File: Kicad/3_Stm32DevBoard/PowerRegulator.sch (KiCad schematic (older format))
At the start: 13 parts, among them J5 PowerTest_PinHeader, J6 9V Power JST XH, U1 AMS1117-5.0, U2 AMS1117-3.3

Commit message: STM32 Dev Board
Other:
- moved on the sheet: J5
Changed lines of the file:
@@
-$EndComp
-$Comp
-L Regulator_Linear:AMS1117-3.3 U?
-U 1 1 5E8DF986
-P 4550 3850
-AR Path="/5E8DF986" Ref="U?"  Part="1"
-AR Path="/5E8D81C7/5E8DF986" Ref="U2"  Part="1"
-F 0 "U2" H 4550 4092 50  0000 C CNN
-F 1 "AMS1117-3.3" H 4550 4001 50  0000 C CNN
-F 2 "Package_TO_SOT_SMD:SOT-223-3_TabPin2" H 4550 4050 50  0001 C CNN
-F 3 "http://www.advanced-monolithic.com/pdf/ds1117.pdf" H 4650 3600 50  0001 C CNN
-	1    4550 3850
-	1    0    0    -1
 $EndComp
 $Comp
@@
 $Comp
 L power:GND #PWR?
-U 1 1 5E8DF9B0
-P 5100 4150
-AR Path="/5E8DF9B0" Ref="#PWR?"  Part="1"
-AR Path="/5E8D81C7/5E8DF9B0" Ref="#PWR016"  Part="1"
-F 0 "#PWR016" H 5100 3900 50  0001 C CNN
-F 1 "GND" H 5105 3977 50  0000 C CNN
-F 2 "" H 5100 4150 50  0001 C CNN
-F 3 "" H 5100 4150 50  0001 C CNN
-	1    5100 4150
-	1    0    0    -1
-$EndComp
-$Comp
-L power:GND #PWR?
 U 1 1 5E8DF9B6
 P 5100 3100
@@
 $EndComp
 Wire Wire Line
-	4850 3850 5100 3850
-Wire Wire Line
 	4850 2800 5100 2800
-Wire Wire Line
-	4250 3850 4100 3850
 Wire Wire Line
 	3550 2800 3550 2850
@@
 	1    0    0    -1
 $EndComp
-$Comp
-L power:GND #PWR?
-U 1 1 5E8DF9C9
-P 4550 4150
-AR Path="/5E8DF9C9" Ref="#PWR?"  Part="1"
-AR Path="/5E8D81C7/5E8DF9C9" Ref="#PWR012"  Part="1"
-F 0 "#PWR012" H 4550 3900 50  0001 C CNN
-F 1 "GND" H 4555 3977 50  0000 C CNN
-F 2 "" H 4550 4150 50  0001 C CNN
-F 3 "" H 4550 4150 50  0001 C CNN
-	1    4550 4150
-	1    0    0    -1
-$EndComp
 Text Notes 3000 3450 0    31   ~ 0
 Vfw = 2 V\n I = (9-2)/1 = 7 mA
 Text Notes 5500 2900 0    31   ~ 0
 5V: LCD: about 60 mA\nPd = (9 V - 5V) * 60 mA = 240 mW\nTj = Ta(max) + Pd * (Thermal Resistance (junction-to-ambient) =\n125 = 30 + Pd * 70 => 1.36 W\nNo heat sink needed
-Text Notes 5500 3900 0    31   ~ 0
-3.3V: STM32: about 100 mA \nPd = (9 V - 3.3V) * 100 mA = 570 mW\nTj = Ta(max) + Pd * (Thermal Resistance (junction-to-ambient) =\n125 = 30 + Pd * 70 => 1.36 W\nNo heat sink needed
-Connection ~ 4100 3850
 $Comp
 L power:+5V #PWR?
@@
 Wire Wire Line
 	4100 2800 4250 2800
-$Comp
-L power:+3V3 #PWR?
-U 1 1 5E8DF9EC
-P 5100 3850
-AR Path="/5E8DF9EC" Ref="#PWR?"  Part="1"
-AR Path="/5E8D81C7/5E8DF9EC" Ref="#PWR015"  Part="1"
-F 0 "#PWR015" H 5100 3700 50  0001 C CNN
-F 1 "+3V3" H 5115 4023 50  0000 C CNN
-F 2 "" H 5100 3850 50  0001 C CNN
-F 3 "" H 5100 3850 50  0001 C CNN
-	1    5100 3850
-	1    0    0    -1
-$EndComp
 Text Notes 3500 1000 0    50   ~ 10
 Power Regulator\n\n
@@
 L power:+5V #PWR0103
 U 1 1 5FACFDD8
-P 1900 3450
-F 0 "#PWR0103" H 1900 3300 50  0001 C CNN
-F 1 "+5V" H 1915 3623 50  0000 C CNN
-F 2 "" H 1900 3450 50  0001 C CNN
-F 3 "" H 1900 3450 50  0001 C CNN
-	1    1900 3450
+P 2050 3700
+F 0 "#PWR0103" H 2050 3550 50  0001 C CNN
+F 1 "+5V" H 2065 3873 50  0000 C CNN
+F 2 "" H 2050 3700 50  0001 C CNN
+F 3 "" H 2050 3700 50  0001 C CNN
+	1    2050 3700
 	1    0    0    -1
 $EndComp
@@
 L power:+3V3 #PWR0104
 U 1 1 5FAD14EB
-P 2100 3550
-F 0 "#PWR0104" H 2100 3400 50  0001 C CNN
-F 1 "+3V3" H 2115 3723 50  0000 C CNN
-F 2 "" H 2100 3550 50  0001 C CNN
-F 3 "" H 2100 3550 50  0001 C CNN
-	1    2100 3550
+P 2250 3800
+F 0 "#PWR0104" H 2250 3650 50  0001 C CNN
+F 1 "+3V3" H 2265 3973 50  0000 C CNN
+F 2 "" H 2250 3800 50  0001 C CNN
+F 3 "" H 2250 3800 50  0001 C CNN
+	1    2250 3800
 	1    0    0    -1
 $EndComp
@@
 L power:GND #PWR?
 U 1 1 5FAD2482
-P 1200 3650
+P 1350 3900
 AR Path="/5FAD2482" Ref="#PWR?"  Part="1"
 AR Path="/5E8D81C7/5FAD2482" Ref="#PWR0105"  Part="1"
-F 0 "#PWR0105" H 1200 3400 50  0001 C CNN
-F 1 "GND" H 1205 3477 50  0000 C CNN
-F 2 "" H 1200 3650 50  0001 C CNN
-F 3 "" H 1200 3650 50  0001 C CNN
-	1    1200 3650
+F 0 "#PWR0105" H 1350 3650 50  0001 C CNN
+F 1 "GND" H 1355 3727 50  0000 C CNN
+F 2 "" H 1350 3900 50  0001 C CNN
+F 3 "" H 1350 3900 50  0001 C CNN
+	1    1350 3900
 	1    0    0    -1
 $EndComp
@@
 $EndComp
 $Comp
-L Device:CP1 C4
-U 1 1 5E99E117
-P 5100 4000
-F 0 "C4" H 5215 4046 50  0000 L CNN
-F 1 "22uF" H 5215 3955 50  0000 L CNN
-F 2 "Diode_SMD:D_SMB_Handsoldering" H 5100 4000 50  0001 C CNN
-F 3 "~" H 5100 4000 50  0001 C CNN
-	1    5100 4000
-	1    0    0    -1
-$EndComp
-Connection ~ 5100 3850
-$Comp
 L Device:CP1 C3
 U 1 1 5E99F224
@@
 L Connector:Conn_01x04_Male J5
 U 1 1 5E90BAA0
-P 1000 3450
-F 0 "J5" H 1108 3731 50  0000 C CNN
-F 1 "PowerTest_PinHeader" H 1108 3640 50  0000 C CNN
-F 2 "Connector_PinHeader_2.54mm:PinHeader_1x04_P2.54mm_Vertical" H 1000 3450 50  0001 C CNN
-F 3 "~" H 1000 3450 50  0001 C CNN
-	1    1000 3450
-	1    0    0    -1
-$EndComp
-Wire Wire Line
-	1200 3550 2100 3550
-Wire Wire Line
-	1900 3450 1200 3450
-Wire Wire Line
-	1200 3350 1700 3350
-$Comp
-L power:+9V #PWR0112
-U 1 1 5EAD02BC
-P 1700 3350
-F 0 "#PWR0112" H 1700 3200 50  0001 C CNN
-F 1 "+9V" H 1715 3523 50  0000 C CNN
-F 2 "" H 1700 3350 50  0001 C CNN
-F 3 "" H 1700 3350 50  0001 C CNN
-	1    1700 3350
-	1    0    0    -1
-$EndComp
+P 1150 3700
+F 0 "J5" H 1258 3981 50  0000 C CNN
+F 1 "PowerTest_PinHeader" H 1258 3890 50  0000 C CNN
+F 2 "Connector_PinHeader_2.54mm:PinHeader_1x04_P2.54mm_Vertical" H 1150 3700 50  0001 C CNN
+F 3 "~" H 1150 3700 50  0001 C CNN
+	1    1150 3700
+	1    0    0    -1
+$EndComp
+Wire Wire Line
+	1350 3800 2250 3800
+Wire Wire Line
+	2050 3700 1350 3700
+Wire Wire Line
+	1350 3600 1850 3600
 Wire Wire Line
 	1250 1250 1550 1250
@@
 Wire Wire Line
 	1550 1250 1700 1250
-Wire Wire Line
-	4100 3850 4100 4550
 Wire Notes Line
 	7400 5200 7400 550
@@
 Text Notes 5500 3100 0    31   ~ 0
 22 uF Tantalum advised ->\n47 uf Tantalum in inventory instead
-Text Notes 5500 4100 0    31   ~ 0
-22 uF Tantalum advised ->\n47 uf Tantalum in inventory instead
 $Comp
 L power:+9V #PWR0114
@@
 	3550 2550 3550 2800
 Wire Wire Line
-	4100 2950 4100 3850
-Wire Wire Line
-	4100 2800 4100 3850
-Wire Wire Line
 	3450 2800 3550 2800
 Text HLabel 3450 2800 0    50   Input ~ 0
@@
 Text Notes 4250 2500 0    50   ~ 0
 Model: BLM21AG102SN1D'\nSpecs: 600 mA, 25% 1 KOhm, 100 MHz, 0805\nAccording AliExpress: 200 mA
+Wire Wire Line
+	4100 2800 4100 3850
+$Comp
+L Device:CP1 C4
+U 1 1 5E99E117
+P 5100 4000
+F 0 "C4" H 5215 4046 50  0000 L CNN
+F 1 "22uF" H 5215 3955 50  0000 L CNN
+F 2 "Diode_SMD:D_SMB_Handsoldering" H 5100 4000 50  0001 C CNN
+F 3 "~" H 5100 4000 50  0001 C CNN
+	1    5100 4000
+	1    0    0    -1
+$EndComp
+$Comp
+L power:+3V3 #PWR?
+U 1 1 5E8DF9EC
+P 5100 3850
+AR Path="/5E8DF9EC" Ref="#PWR?"  Part="1"
+AR Path="/5E8D81C7/5E8DF9EC" Ref="#PWR015"  Part="1"
+F 0 "#PWR015" H 5100 3700 50  0001 C CNN
+F 1 "+3V3" H 5115 4023 50  0000 C CNN
+F 2 "" H 5100 3850 50  0001 C CNN
+F 3 "" H 5100 3850 50  0001 C CNN
+	1    5100 3850
+	1    0    0    -1
+$EndComp
+$Comp
+L power:GND #PWR?
+U 1 1 5E8DF9C9
+P 4550 4150
+AR Path="/5E8DF9C9" Ref="#PWR?"  Part="1"
+AR Path="/5E8D81C7/5E8DF9C9" Ref="#PWR012"  Part="1"
+F 0 "#PWR012" H 4550 3900 50  0001 C CNN
+F 1 "GND" H 4555 3977 50  0000 C CNN
+F 2 "" H 4550 4150 50  0001 C CNN
+F 3 "" H 4550 4150 50  0001 C CNN
+	1    4550 4150
+	1    0    0    -1
+$EndComp
+Wire Wire Line
+	4100 2950 4100 3850
+Wire Wire Line
+	4100 3850 4100 4550
+Connection ~ 4100 3850
+Wire Wire Line
+	4250 3850 4100 3850
+Connection ~ 5100 3850
+Wire Wire Line
+	4850 3850 5100 3850
+$Comp
+L power:GND #PWR?
+U 1 1 5E8DF9B0
+P 5100 4150
+AR Path="/5E8DF9B0" Ref="#PWR?"  Part="1"
+AR Path="/5E8D81C7/5E8DF9B0" Ref="#PWR016"  Part="1"
+F 0 "#PWR016" H 5100 3900 50  0001 C CNN
+F 1 "GND" H 5105 3977 50  0000 C CNN
+F 2 "" H 5100 4150 50  0001 C CNN
+F 3 "" H 5100 4150 50  0001 C CNN
+	1    5100 4150
+	1    0    0    -1
+$EndComp
+$Comp
+L Regulator_Linear:AMS1117-3.3 U?
+U 1 1 5E8DF986
+P 4550 3850
+AR Path="/5E8DF986" Ref="U?"  Part="1"
+AR Path="/5E8D81C7/5E8DF986" Ref="U2"  Part="1"
+F 0 "U2" H 4550 4092 50  0000 C CNN
+F 1 "AMS1117-3.3" H 4550 4001 50  0000 C CNN
+F 2 "Package_TO_SOT_SMD:SOT-223-3_TabPin2" H 4550 4050 50  0001 C CNN
+F 3 "http://www.advanced-monolithic.com/pdf/ds1117.pdf" H 4650 3600 50  0001 C CNN
+	1    4550 3850
+	1    0    0    -1
+$EndComp
+Text Notes 5500 4100 0    31   ~ 0
+22 uF Tantalum advised ->\n47 uf Tantalum in inventory instead
+Text Notes 5500 3900 0    31   ~ 0
+3.3V: STM32: about 100 mA \nPd = (9 V - 3.3V) * 100 mA = 570 mW\nTj = Ta(max) + Pd * (Thermal Resistance (junction-to-ambient) =\n125 = 30 + Pd * 70 => 1.36 W\nNo heat sink needed
+Text HLabel 1850 3600 1    50   Input ~ 0
++9V_SAFE
 $EndSCHEMATC

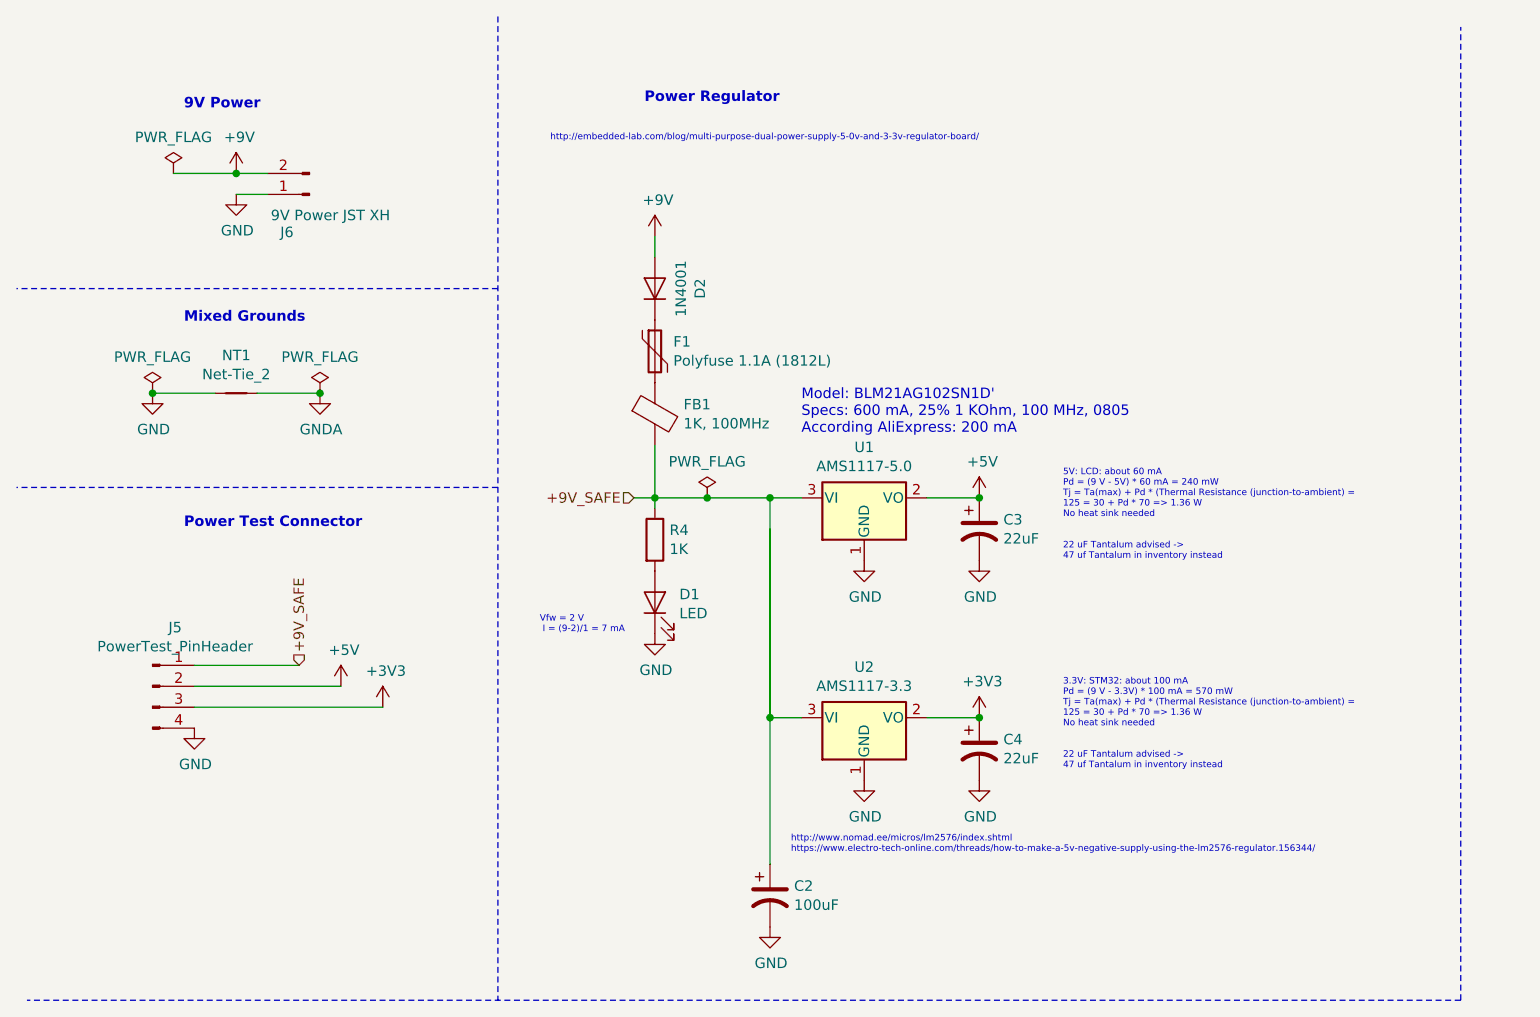
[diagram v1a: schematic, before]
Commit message: Remove 3V3 voltage regulation (get from STM32 5V)
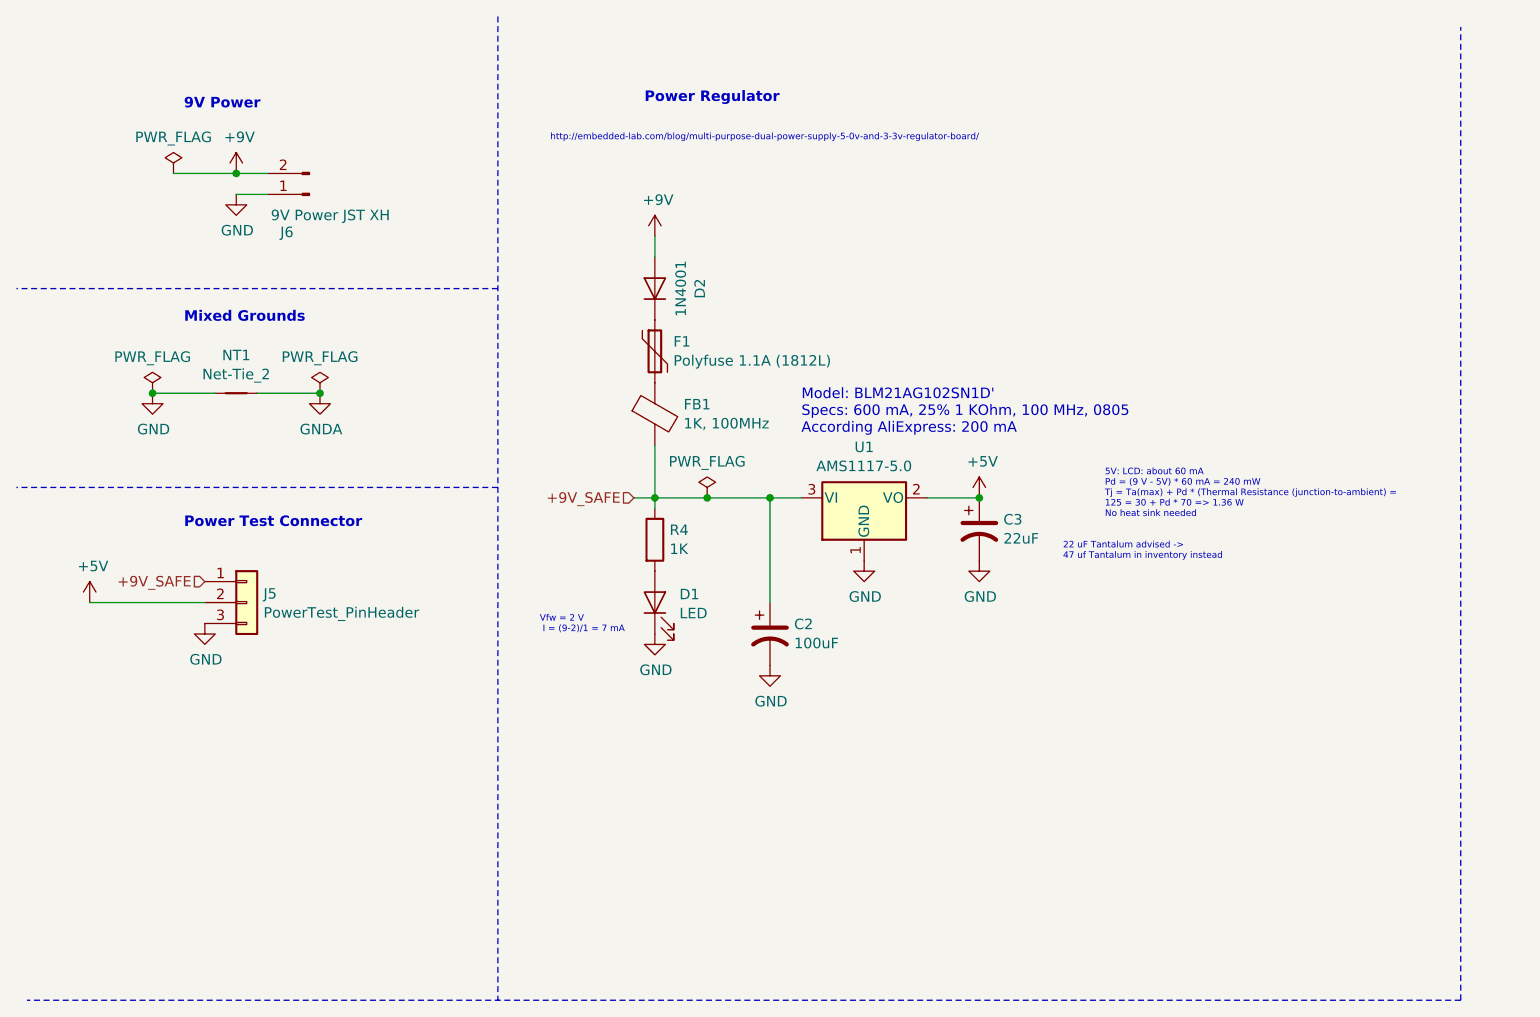
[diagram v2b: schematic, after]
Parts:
- removed C4: 22uF, Diode_SMD:D_SMB_Handsoldering, symbol Device:CP1
- removed J5: PowerTest_PinHeader, Connector_PinHeader_2.54mm:PinHeader_1x04_P2.54mm_Vertical, symbol Connector:Conn_01x04_Male
- removed U2: AMS1117-3.3, Package_TO_SOT_SMD:SOT-223-3_TabPin2, symbol Regulator_Linear:AMS1117-3.3
- added J5: PowerTest_PinHeader, Connector_PinHeader_2.54mm:PinHeader_1x03_P2.54mm_Vertical, symbol Connector_Generic:Conn_01x03
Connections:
- net labels removed: +3V3
- wire segments 21 -> 15
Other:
- note removed: "3.3V: STM32: about 100 mA \nPd = (9 V - 3.3V) * 100 mA = 570 mW\nTj = Ta(max) + Pd * (Thermal Resistance (junction-to-ambient) =\n125 = 30 + Pd * 70 => 1.36 W\nNo heat sink needed"
- note removed: "http://www.nomad.ee/micros/lm2576/index.shtml"
- note removed: "https://www.electro-tech-online.com/threads/how-to-make-a-5v-negative-supply-using-the-lm2576-regulator.156344/"
- moved on the sheet: C2
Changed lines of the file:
@@
 L power:GND #PWR?
 U 1 1 5E8DF9AA
-P 4100 4850
+P 4100 3600
 AR Path="/5E8DF9AA" Ref="#PWR?"  Part="1"
 AR Path="/5E8D81C7/5E8DF9AA" Ref="#PWR010"  Part="1"
-F 0 "#PWR010" H 4100 4600 50  0001 C CNN
-F 1 "GND" H 4105 4677 50  0000 C CNN
-F 2 "" H 4100 4850 50  0001 C CNN
-F 3 "" H 4100 4850 50  0001 C CNN
-	1    4100 4850
+F 0 "#PWR010" H 4100 3350 50  0001 C CNN
+F 1 "GND" H 4105 3427 50  0000 C CNN
+F 2 "" H 4100 3600 50  0001 C CNN
+F 3 "" H 4100 3600 50  0001 C CNN
+	1    4100 3600
 	1    0    0    -1
 $EndComp
@@
 Text Notes 3000 3450 0    31   ~ 0
 Vfw = 2 V\n I = (9-2)/1 = 7 mA
-Text Notes 5500 2900 0    31   ~ 0
+Text Notes 5700 2900 0    31   ~ 0
 5V: LCD: about 60 mA\nPd = (9 V - 5V) * 60 mA = 240 mW\nTj = Ta(max) + Pd * (Thermal Resistance (junction-to-ambient) =\n125 = 30 + Pd * 70 => 1.36 W\nNo heat sink needed
 $Comp
@@
 $EndComp
 $Comp
-L power:+5V #PWR0103
-U 1 1 5FACFDD8
-P 2050 3700
-F 0 "#PWR0103" H 2050 3550 50  0001 C CNN
-F 1 "+5V" H 2065 3873 50  0000 C CNN
-F 2 "" H 2050 3700 50  0001 C CNN
-F 3 "" H 2050 3700 50  0001 C CNN
-	1    2050 3700
-	1    0    0    -1
-$EndComp
-$Comp
-L power:+3V3 #PWR0104
-U 1 1 5FAD14EB
-P 2250 3800
-F 0 "#PWR0104" H 2250 3650 50  0001 C CNN
-F 1 "+3V3" H 2265 3973 50  0000 C CNN
-F 2 "" H 2250 3800 50  0001 C CNN
-F 3 "" H 2250 3800 50  0001 C CNN
-	1    2250 3800
-	1    0    0    -1
-$EndComp
-$Comp
 L power:GND #PWR?
 U 1 1 5FAD2482
-P 1350 3900
+P 1400 3400
 AR Path="/5FAD2482" Ref="#PWR?"  Part="1"
 AR Path="/5E8D81C7/5FAD2482" Ref="#PWR0105"  Part="1"
-F 0 "#PWR0105" H 1350 3650 50  0001 C CNN
-F 1 "GND" H 1355 3727 50  0000 C CNN
-F 2 "" H 1350 3900 50  0001 C CNN
-F 3 "" H 1350 3900 50  0001 C CNN
-	1    1350 3900
+F 0 "#PWR0105" H 1400 3150 50  0001 C CNN
+F 1 "GND" H 1405 3227 50  0000 C CNN
+F 2 "" H 1400 3400 50  0001 C CNN
+F 3 "" H 1400 3400 50  0001 C CNN
+	1    1400 3400
 	1    0    0    -1
 $EndComp
@@
 L Device:CP1 C2
 U 1 1 5E99F989
-P 4100 4700
-F 0 "C2" H 4215 4746 50  0000 L CNN
-F 1 "100uF" H 4215 4655 50  0000 L CNN
-F 2 "Capacitor_THT:CP_Radial_D5.0mm_P2.50mm" H 4100 4700 50  0001 C CNN
-F 3 "~" H 4100 4700 50  0001 C CNN
-	1    4100 4700
+P 4100 3450
+F 0 "C2" H 4215 3496 50  0000 L CNN
+F 1 "100uF" H 4215 3405 50  0000 L CNN
+F 2 "Capacitor_THT:CP_Radial_D5.0mm_P2.50mm" H 4100 3450 50  0001 C CNN
+F 3 "~" H 4100 3450 50  0001 C CNN
+	1    4100 3450
 	1    0    0    -1
 $EndComp
@@
 Wire Notes Line
 	2800 2750 500  2750
-Text Notes 4200 4500 0    31   ~ 0
-https://www.electro-tech-online.com/threads/how-to-make-a-5v-negative-supply-using-the-lm2576-regulator.156344/
-Text Notes 4200 4450 0    31   ~ 0
-http://www.nomad.ee/micros/lm2576/index.shtml
-$Comp
-L Connector:Conn_01x04_Male J5
-U 1 1 5E90BAA0
-P 1150 3700
-F 0 "J5" H 1258 3981 50  0000 C CNN
-F 1 "PowerTest_PinHeader" H 1258 3890 50  0000 C CNN
-F 2 "Connector_PinHeader_2.54mm:PinHeader_1x04_P2.54mm_Vertical" H 1150 3700 50  0001 C CNN
-F 3 "~" H 1150 3700 50  0001 C CNN
-	1    1150 3700
-	1    0    0    -1
-$EndComp
-Wire Wire Line
-	1350 3800 2250 3800
-Wire Wire Line
-	2050 3700 1350 3700
-Wire Wire Line
-	1350 3600 1850 3600
 Wire Wire Line
 	1250 1250 1550 1250
@@
 Text Notes 4250 2500 0    50   ~ 0
 Model: BLM21AG102SN1D'\nSpecs: 600 mA, 25% 1 KOhm, 100 MHz, 0805\nAccording AliExpress: 200 mA
-Wire Wire Line
-	4100 2800 4100 3850
-$Comp
-L Device:CP1 C4
-U 1 1 5E99E117
-P 5100 4000
-F 0 "C4" H 5215 4046 50  0000 L CNN
-F 1 "22uF" H 5215 3955 50  0000 L CNN
-F 2 "Diode_SMD:D_SMB_Handsoldering" H 5100 4000 50  0001 C CNN
-F 3 "~" H 5100 4000 50  0001 C CNN
-	1    5100 4000
-	1    0    0    -1
-$EndComp
-$Comp
-L power:+3V3 #PWR?
-U 1 1 5E8DF9EC
-P 5100 3850
-AR Path="/5E8DF9EC" Ref="#PWR?"  Part="1"
-AR Path="/5E8D81C7/5E8DF9EC" Ref="#PWR015"  Part="1"
-F 0 "#PWR015" H 5100 3700 50  0001 C CNN
-F 1 "+3V3" H 5115 4023 50  0000 C CNN
-F 2 "" H 5100 3850 50  0001 C CNN
-F 3 "" H 5100 3850 50  0001 C CNN
-	1    5100 3850
-	1    0    0    -1
-$EndComp
-$Comp
-L power:GND #PWR?
-U 1 1 5E8DF9C9
-P 4550 4150
-AR Path="/5E8DF9C9" Ref="#PWR?"  Part="1"
-AR Path="/5E8D81C7/5E8DF9C9" Ref="#PWR012"  Part="1"
-F 0 "#PWR012" H 4550 3900 50  0001 C CNN
-F 1 "GND" H 4555 3977 50  0000 C CNN
-F 2 "" H 4550 4150 50  0001 C CNN
-F 3 "" H 4550 4150 50  0001 C CNN
-	1    4550 4150
-	1    0    0    -1
-$EndComp
-Wire Wire Line
-	4100 2950 4100 3850
-Wire Wire Line
-	4100 3850 4100 4550
-Connection ~ 4100 3850
-Wire Wire Line
-	4250 3850 4100 3850
-Connection ~ 5100 3850
-Wire Wire Line
-	4850 3850 5100 3850
-$Comp
-L power:GND #PWR?
-U 1 1 5E8DF9B0
-P 5100 4150
-AR Path="/5E8DF9B0" Ref="#PWR?"  Part="1"
-AR Path="/5E8D81C7/5E8DF9B0" Ref="#PWR016"  Part="1"
-F 0 "#PWR016" H 5100 3900 50  0001 C CNN
-F 1 "GND" H 5105 3977 50  0000 C CNN
-F 2 "" H 5100 4150 50  0001 C CNN
-F 3 "" H 5100 4150 50  0001 C CNN
-	1    5100 4150
-	1    0    0    -1
-$EndComp
-$Comp
-L Regulator_Linear:AMS1117-3.3 U?
-U 1 1 5E8DF986
-P 4550 3850
-AR Path="/5E8DF986" Ref="U?"  Part="1"
-AR Path="/5E8D81C7/5E8DF986" Ref="U2"  Part="1"
-F 0 "U2" H 4550 4092 50  0000 C CNN
-F 1 "AMS1117-3.3" H 4550 4001 50  0000 C CNN
-F 2 "Package_TO_SOT_SMD:SOT-223-3_TabPin2" H 4550 4050 50  0001 C CNN
-F 3 "http://www.advanced-monolithic.com/pdf/ds1117.pdf" H 4650 3600 50  0001 C CNN
-	1    4550 3850
-	1    0    0    -1
-$EndComp
-Text Notes 5500 4100 0    31   ~ 0
-22 uF Tantalum advised ->\n47 uf Tantalum in inventory instead
-Text Notes 5500 3900 0    31   ~ 0
-3.3V: STM32: about 100 mA \nPd = (9 V - 3.3V) * 100 mA = 570 mW\nTj = Ta(max) + Pd * (Thermal Resistance (junction-to-ambient) =\n125 = 30 + Pd * 70 => 1.36 W\nNo heat sink needed
-Text HLabel 1850 3600 1    50   Input ~ 0
+Text HLabel 1400 3200 0    50   Input ~ 0
 +9V_SAFE
+Wire Wire Line
+	4100 2800 4100 3300
+$Comp
+L Connector_Generic:Conn_01x03 J5
+U 1 1 5F0130BE
+P 1600 3300
+F 0 "J5" H 1680 3342 50  0000 L CNN
+F 1 "PowerTest_PinHeader" H 1680 3251 50  0000 L CNN
+F 2 "Connector_PinHeader_2.54mm:PinHeader_1x03_P2.54mm_Vertical" H 1600 3300 50  0001 C CNN
+F 3 "~" H 1600 3300 50  0001 C CNN
+	1    1600 3300
+	1    0    0    -1
+$EndComp
+$Comp
+L power:+5V #PWR0103
+U 1 1 5F0147F5
+P 850 3300
+F 0 "#PWR0103" H 850 3150 50  0001 C CNN
+F 1 "+5V" H 865 3473 50  0000 C CNN
+F 2 "" H 850 3300 50  0001 C CNN
+F 3 "" H 850 3300 50  0001 C CNN
+	1    850  3300
+	1    0    0    -1
+$EndComp
+Wire Wire Line
+	1400 3300 850  3300
 $EndSCHEMATC
